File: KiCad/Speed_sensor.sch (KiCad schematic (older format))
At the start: 20 parts

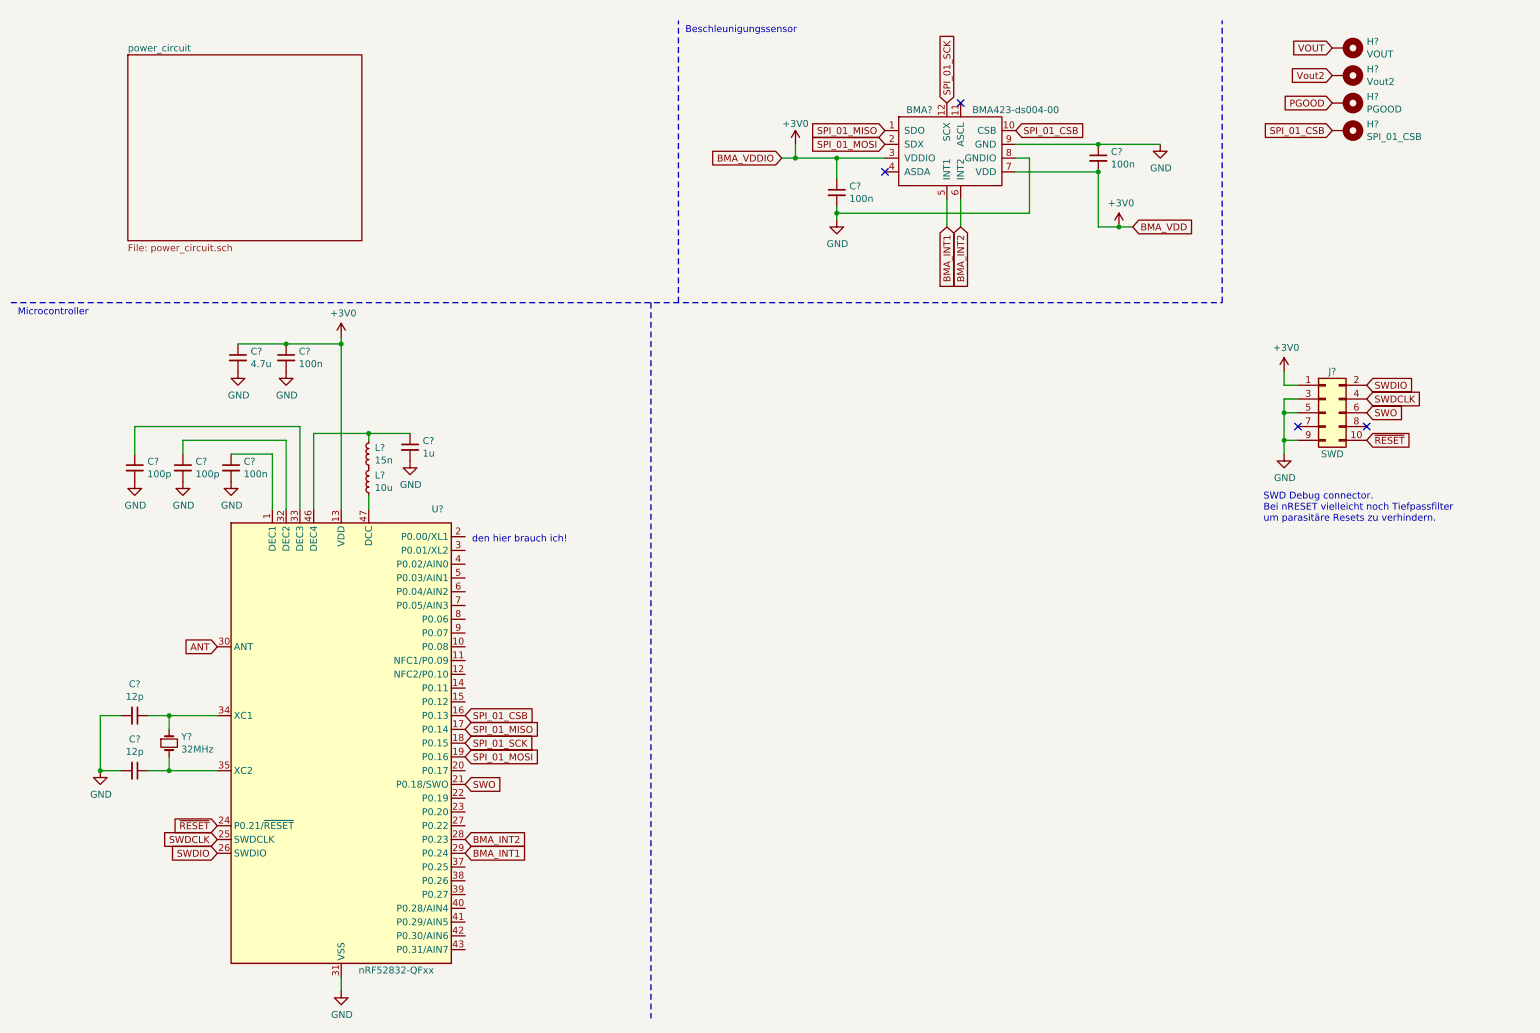
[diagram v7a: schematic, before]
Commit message: power circuit übersichtlicher gemacht, low battery voltage detection verändert.
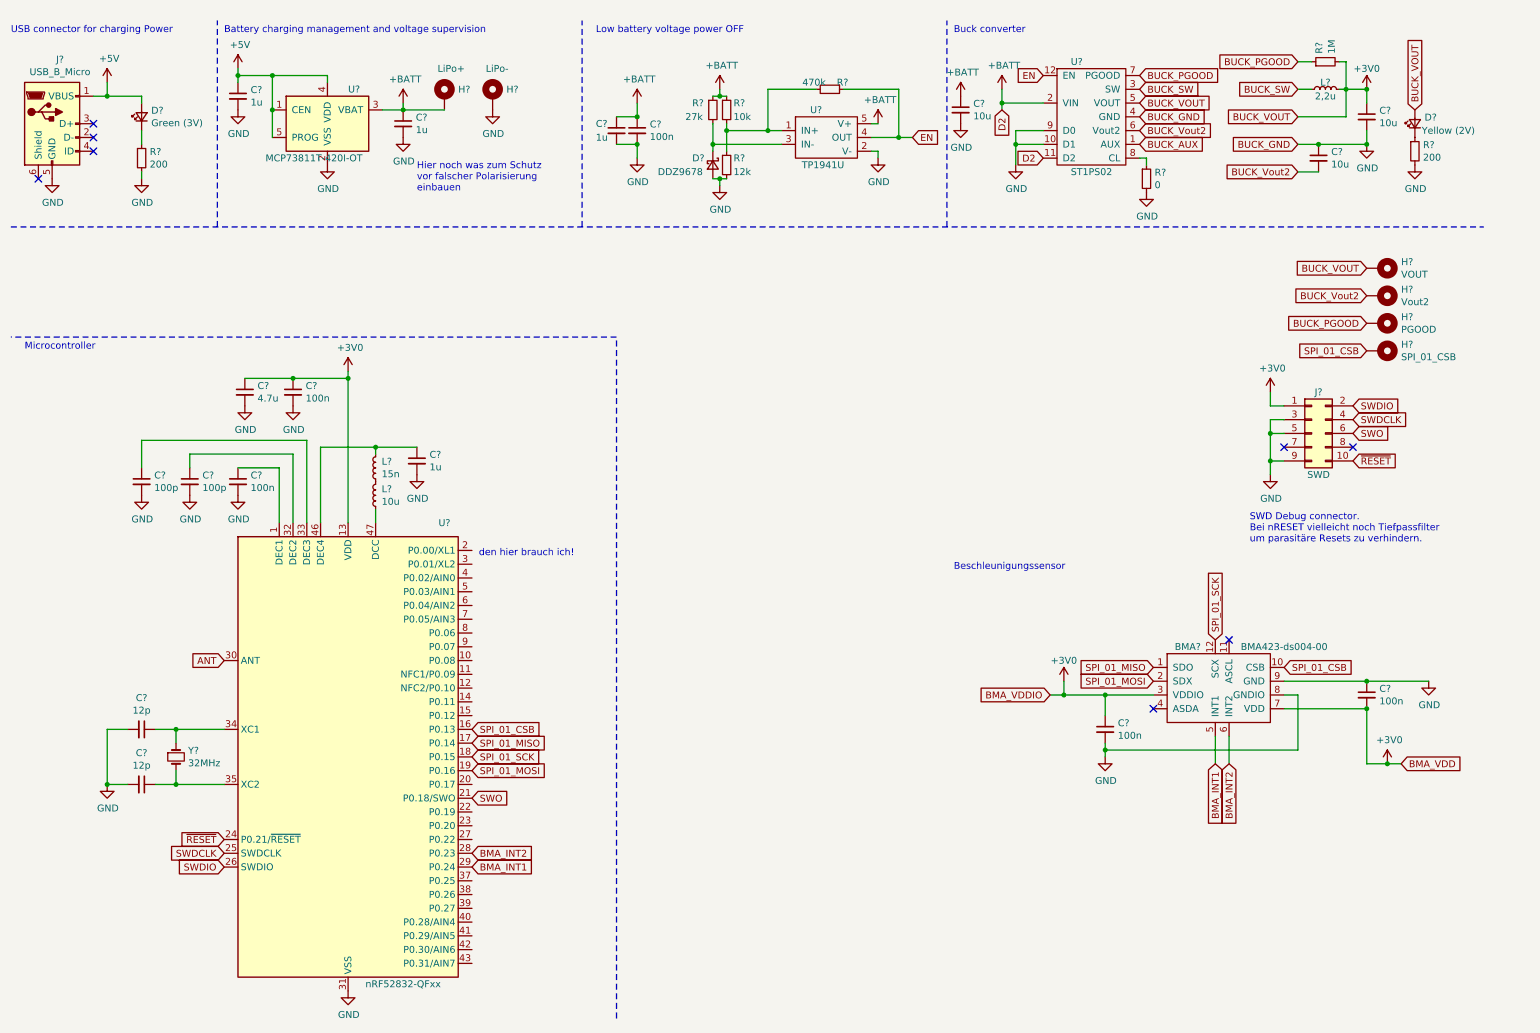
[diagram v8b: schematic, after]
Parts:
- added C? (x3): 1u, symbol Device:C_Small
- added C?: 100n, symbol Device:C_Small
- added C? (x3): 10u, symbol Device:C_Small
- added D?: Green (3V), symbol Device:LED_Small
- added D?: Yellow (2V), symbol Device:LED_Small
- added D?: DDZ9678, symbol Device:D_Schottky_Small
- added H?: LiPo+, symbol Mechanical:MountingHole_Pad
- added H?: LiPo-, symbol Mechanical:MountingHole_Pad
- added J?: USB_B_Micro, symbol Connector:USB_B_Micro
- added L?: 2,2u, symbol Device:L_Small
- added R? (x2): 200, symbol Device:R_Small
- added R?: 27k, symbol Device:R_Small
- added R?: 10k, symbol Device:R_Small
- added R?: 12k, symbol Device:R_Small
- added R?: 470k, symbol Device:R_Small
- added R?: 0, symbol Device:R_Small
- added R?: 1M, symbol Device:R_Small
- added U?: MCP73811T-420I-OT, Package_TO_SOT_SMD:SOT-23-5, symbol Battery_Management:MCP73811T-420I-OT
- added U?: TP1941U, symbol Nils_KiCADLibrary:TP1941U
- added U?: ST1PS02, symbol Nils_KiCADLibrary:ST1PS02
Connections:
- net VOUT is gone; now on net +3V0: H?.1
- net +3V0: now also C?.1, D?.2 (A), L?.2, R?.2, U?.5 (VOUT)
- net GND: now also C?.1, C?.2, C?.2, C?.2, C?.2, C?.2, C?.2, D?.2 (A), H?.1, J?.5 (GND), R?.2, R?.2, R?.2, R?.2, U?.10 (D1), U?.2 (V-), U?.2 (VSS), U?.4 (GND), U?.9 (D0)
- net PGOOD renamed BUCK_PGOOD
- net BUCK_PGOOD: now also R?.1, U?.7 (PGOOD)
- net Vout2 renamed BUCK_Vout2
- net BUCK_Vout2: now also C?.2, U?.6 (Vout2)
- new net: D?.1 (K), R?.1 (x2)
- new net: D?.1 (K), R?.2, U?.3 (IN-)
- new net: R?.1, R?.2, R?.2, U?.1 (IN+)
- new net: R?.1, U?.8 (CL)
- new net +5V: C?.1, D?.2 (A), J?.1 (VBUS), U?.1 (CEN), U?.4 (VDD), U?.5 (PROG)
- new net +BATT: C?.1, C?.1, C?.1, C?.1, H?.1, R?.1, R?.1, U?.11 (D2), U?.2 (VIN), U?.3 (VBAT), U?.5 (V+)
- new net BUCK_AUX: U?.1 (AUX)
- new net BUCK_SW: L?.1, U?.3 (SW)
- new net EN: R?.1, U?.12 (EN), U?.4 (OUT)
- no-connect marks 4 -> 8
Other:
- note added: "Battery charging management and voltage supervision"
- note added: "Buck converter"
- note added: "Hier noch was zum Schutz\nvor falscher Polarisierung\neinbauen"
- note added: "Low battery voltage power OFF"
- note added: "USB connector for charging Power"
- moved on the sheet: BMA?, C?, H?, J?, L?, U?, Y?
